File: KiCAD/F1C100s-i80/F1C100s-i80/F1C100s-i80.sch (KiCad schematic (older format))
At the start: 98 parts, among them J1 LCD_I8080_CONNECTOR_16x2-DIP, J10 USB_B_Micro, J2 Key Export, J3 SPK, J4 LRADC, J5 UART, J6 Touch, J7 Power, J8 Micro_SD_Card, J9 USB_A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

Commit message: c100s
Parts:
- J2: footprint Connector_PinHeader_2.54mm:PinHeader_1x08_P2.54mm_Horizontal -> Connector_PinHeader_2.54mm:PinHeader_1x07_P2.54mm_Horizontal
- R25, R26, R28, R29: value 0R -> 22R
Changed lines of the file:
@@
 P 10250 4750
 F 0 "R25" V 10200 4650 50  0000 C CNN
-F 1 "0R" V 10250 4750 50  0000 C CNN
+F 1 "22R" V 10250 4750 50  0000 C CNN
 F 2 "Resistor_SMD:R_0603_1608Metric_Pad1.05x0.95mm_HandSolder" H 10250 4750 50  0001 C CNN
 F 3 "~" H 10250 4750 50  0001 C CNN
@@
 P 10450 5550
 F 0 "R28" V 10400 5450 50  0000 C CNN
-F 1 "0R" V 10450 5550 50  0000 C CNN
+F 1 "22R" V 10450 5550 50  0000 C CNN
 F 2 "Resistor_SMD:R_0603_1608Metric_Pad1.05x0.95mm_HandSolder" H 10450 5550 50  0001 C CNN
 F 3 "~" H 10450 5550 50  0001 C CNN
@@
 P 10450 5650
 F 0 "R29" V 10400 5550 50  0000 C CNN
-F 1 "0R" V 10450 5650 50  0000 C CNN
+F 1 "22R" V 10450 5650 50  0000 C CNN
 F 2 "Resistor_SMD:R_0603_1608Metric_Pad1.05x0.95mm_HandSolder" H 10450 5650 50  0001 C CNN
 F 3 "~" H 10450 5650 50  0001 C CNN
@@
 P 10250 4850
 F 0 "R26" V 10200 4750 50  0000 C CNN
-F 1 "0R" V 10250 4850 50  0000 C CNN
+F 1 "22R" V 10250 4850 50  0000 C CNN
 F 2 "Resistor_SMD:R_0603_1608Metric_Pad1.05x0.95mm_HandSolder" H 10250 4850 50  0001 C CNN
 F 3 "~" H 10250 4850 50  0001 C CNN
@@
 F 0 "J2" H 6950 3300 50  0000 C CNN
 F 1 "Key Export" H 7200 2450 50  0000 C CNN
-F 2 "Connector_PinHeader_2.54mm:PinHeader_1x08_P2.54mm_Horizontal" H 7000 2950 50  0001 C CNN
+F 2 "Connector_PinHeader_2.54mm:PinHeader_1x07_P2.54mm_Horizontal" H 7000 2950 50  0001 C CNN
 F 3 "~" H 7000 2950 50  0001 C CNN
 	1    7000 2950

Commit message: c100s&f40x
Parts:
- BT1: footprint Battery:BatteryHolder_Keystone_3000_1x12mm -> qmechanics:CR1220-2
- J2: footprint Connector_PinHeader_2.54mm:PinHeader_1x07_P2.54mm_Horizontal -> Connector_PinHeader_2.54mm:PinHeader_1x08_P2.54mm_Horizontal
- J9: footprint qconnectors:USB-AF -> qconnectors:USB-AF90
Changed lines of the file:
@@
 F 0 "J9" H 11200 5100 50  0000 R CNN
 F 1 "USB_A" H 11250 4400 50  0000 R CNN
-F 2 "qconnectors:USB-AF" H 11100 4700 50  0001 C CNN
+F 2 "qconnectors:USB-AF90" H 11100 4700 50  0001 C CNN
 F 3 " ~" H 11100 4700 50  0001 C CNN
 	1    10950 4750
@@
 F 0 "BT1" H 6458 4946 50  0000 L CNN
 F 1 "Battery" H 6458 4855 50  0000 L CNN
-F 2 "Battery:BatteryHolder_Keystone_3000_1x12mm" V 6350 4960 50  0001 C CNN
+F 2 "qmechanics:CR1220-2" V 6350 4960 50  0001 C CNN
 F 3 "~" V 6350 4960 50  0001 C CNN
 	1    6350 4900
@@
 F 0 "J2" H 6950 3300 50  0000 C CNN
 F 1 "Key Export" H 7200 2450 50  0000 C CNN
-F 2 "Connector_PinHeader_2.54mm:PinHeader_1x07_P2.54mm_Horizontal" H 7000 2950 50  0001 C CNN
+F 2 "Connector_PinHeader_2.54mm:PinHeader_1x08_P2.54mm_Horizontal" H 7000 2950 50  0001 C CNN
 F 3 "~" H 7000 2950 50  0001 C CNN
 	1    7000 2950

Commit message: 修改DCDC部分
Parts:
- C21, C22, C23: footprint Capacitor_SMD:C_0603_1608Metric_Pad1.05x0.95mm_HandSolder -> Capacitor_SMD:C_1206_3216Metric_Pad1.42x1.75mm_HandSolder
- J10: footprint Connector_USB:USB_Micro-B_Wuerth_629105150521 -> qconnectors:USB_Micro
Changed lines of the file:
@@
 EESchema Schematic File Version 4
-LIBS:F1C100s-i80-cache
 EELAYER 30 0
 EELAYER END
@@
 F 0 "C21" H 9100 900 50  0000 L CNN
 F 1 "10uF" H 9100 800 50  0000 L CNN
-F 2 "Capacitor_SMD:C_0603_1608Metric_Pad1.05x0.95mm_HandSolder" H 9100 850 50  0001 C CNN
+F 2 "Capacitor_SMD:C_1206_3216Metric_Pad1.42x1.75mm_HandSolder" H 9100 850 50  0001 C CNN
 F 3 "~" H 9100 850 50  0001 C CNN
 	1    9100 850
@@
 F 0 "C22" H 9100 1400 50  0000 L CNN
 F 1 "10uF" H 9100 1300 50  0000 L CNN
-F 2 "Capacitor_SMD:C_0603_1608Metric_Pad1.05x0.95mm_HandSolder" H 9100 1350 50  0001 C CNN
+F 2 "Capacitor_SMD:C_1206_3216Metric_Pad1.42x1.75mm_HandSolder" H 9100 1350 50  0001 C CNN
 F 3 "~" H 9100 1350 50  0001 C CNN
 	1    9100 1350
@@
 F 0 "C23" H 9100 1900 50  0000 L CNN
 F 1 "10uF" H 9100 1800 50  0000 L CNN
-F 2 "Capacitor_SMD:C_0603_1608Metric_Pad1.05x0.95mm_HandSolder" H 9100 1850 50  0001 C CNN
+F 2 "Capacitor_SMD:C_1206_3216Metric_Pad1.42x1.75mm_HandSolder" H 9100 1850 50  0001 C CNN
 F 3 "~" H 9100 1850 50  0001 C CNN
 	1    9100 1850
@@
 F 0 "J10" H 11200 5900 50  0000 R CNN
 F 1 "USB_B_Micro" H 11500 5200 50  0000 R CNN
-F 2 "Connector_USB:USB_Micro-B_Wuerth_629105150521" H 11100 5500 50  0001 C CNN
+F 2 "qconnectors:USB_Micro" H 11100 5500 50  0001 C CNN
 F 3 "~" H 11100 5500 50  0001 C CNN
 	1    10950 5550

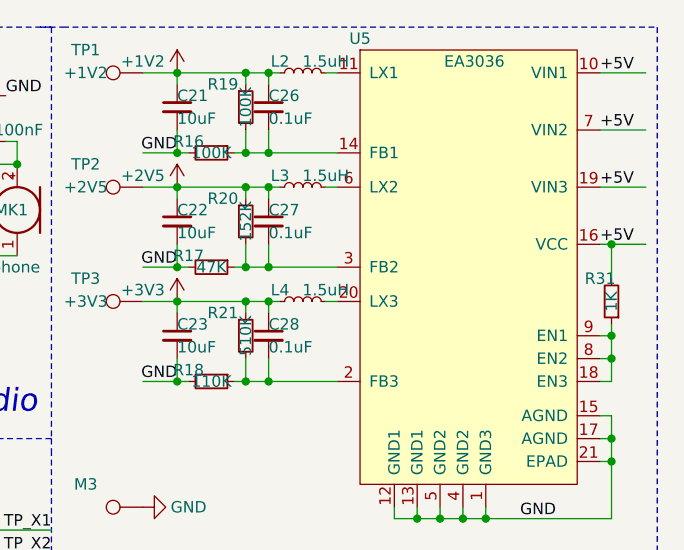
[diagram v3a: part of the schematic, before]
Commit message: 更改C100s走线
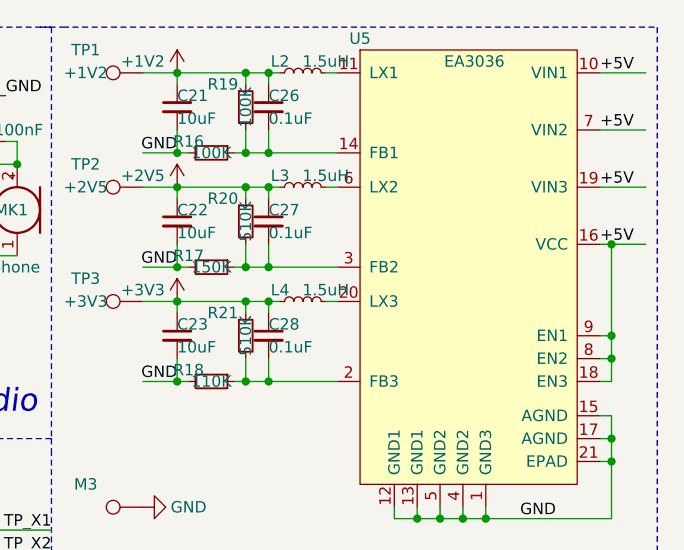
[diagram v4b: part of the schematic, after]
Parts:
- removed R31: 1K, Resistor_SMD:R_0603_1608Metric_Pad1.05x0.95mm_HandSolder, symbol Device:R_Small
- R17: value 47K -> 150K
- R20: value 152K -> 510K
- RN1: footprint Resistor_SMD:R_Cat16-4 -> Resistor_SMD:R_Array_Convex_4x0603
- U5: footprint qchip:EA3036-QFN-20_EP_3.55x3.55_Pitch0.4mm -> qchip:EA3036-QFN-20_EP_3.55x3.55_Pitch0.4mm_Handsoldering
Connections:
- wire segments 325 -> 324
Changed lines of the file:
@@
 F 0 "U5" H 9900 3150 50  0000 C CNN
 F 1 "EA3036" H 10400 3050 50  0000 C CNN
-F 2 "qchip:EA3036-QFN-20_EP_3.55x3.55_Pitch0.4mm" H 8250 1850 50  0001 C CNN
+F 2 "qchip:EA3036-QFN-20_EP_3.55x3.55_Pitch0.4mm_Handsoldering" H 8250 1850 50  0001 C CNN
 F 3 "" H 8250 1850 50  0001 C CNN
 	1    10350 1850
 	1    0    0    -1
 $EndComp
-$Comp
-L Device:R_Small R31
-U 1 1 5DF74049
-P 11000 1700
-F 0 "R31" H 11050 1600 50  0000 C CNN
-F 1 "1K" V 11000 1700 50  0000 C CNN
-F 2 "Resistor_SMD:R_0603_1608Metric_Pad1.05x0.95mm_HandSolder" H 11000 1700 50  0001 C CNN
-F 3 "~" H 11000 1700 50  0001 C CNN
-	1    11000 1700
-	-1   0    0    1
-$EndComp
 Wire Wire Line
 	10950 1850 11000 1850
@@
 Wire Wire Line
 	11000 1950 11000 1850
-Wire Wire Line
-	11000 1850 11000 1800
 Text Label 10950 1200 0    50   ~ 0
 +5V
@@
 Text Label 10950 1450 0    50   ~ 0
 +5V
-Wire Wire Line
-	11000 1600 11000 1450
 Wire Wire Line
 	10950 1450 11000 1450
@@
 P 9400 1350
 F 0 "R20" H 9300 1450 50  0000 C CNN
-F 1 "152K" V 9400 1350 50  0000 C CNN
+F 1 "510K" V 9400 1350 50  0000 C CNN
 F 2 "Resistor_SMD:R_0603_1608Metric_Pad1.05x0.95mm_HandSolder" H 9400 1350 50  0001 C CNN
 F 3 "~" H 9400 1350 50  0001 C CNN
@@
 P 9250 1550
 F 0 "R17" V 9200 1450 50  0000 C CNN
-F 1 "47K" V 9250 1550 50  0000 C CNN
+F 1 "150K" V 9250 1550 50  0000 C CNN
 F 2 "Resistor_SMD:R_0603_1608Metric_Pad1.05x0.95mm_HandSolder" H 9250 1550 50  0001 C CNN
 F 3 "~" H 9250 1550 50  0001 C CNN
@@
 F 0 "RN1" V 8450 4500 50  0000 C CNN
 F 1 "47K" V 8450 4650 50  0000 C CNN
-F 2 "Resistor_SMD:R_Cat16-4" V 9025 4650 50  0001 C CNN
+F 2 "Resistor_SMD:R_Array_Convex_4x0603" V 9025 4650 50  0001 C CNN
 F 3 "~" H 8750 4650 50  0001 C CNN
 	1    8750 4650
@@
 Text Label 7250 2950 0    50   ~ 0
 KEYX
+Wire Wire Line
+	11000 1450 11000 1850
 $EndSCHEMATC

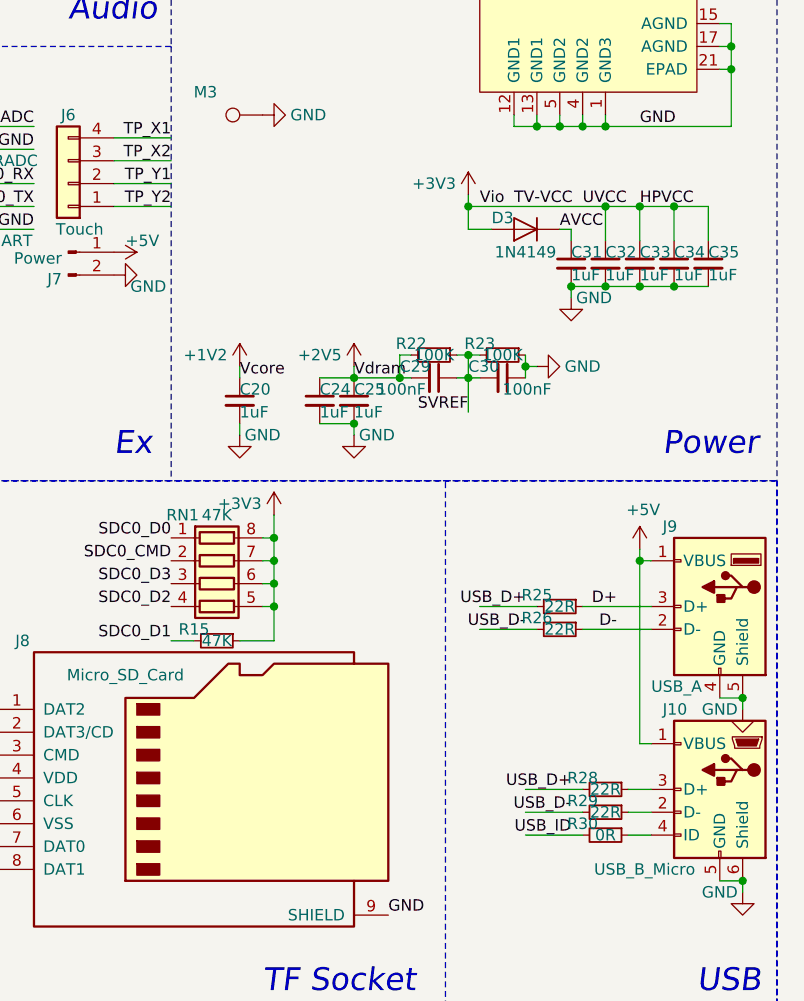
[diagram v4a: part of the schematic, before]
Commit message: 修改排阻为0603电阻
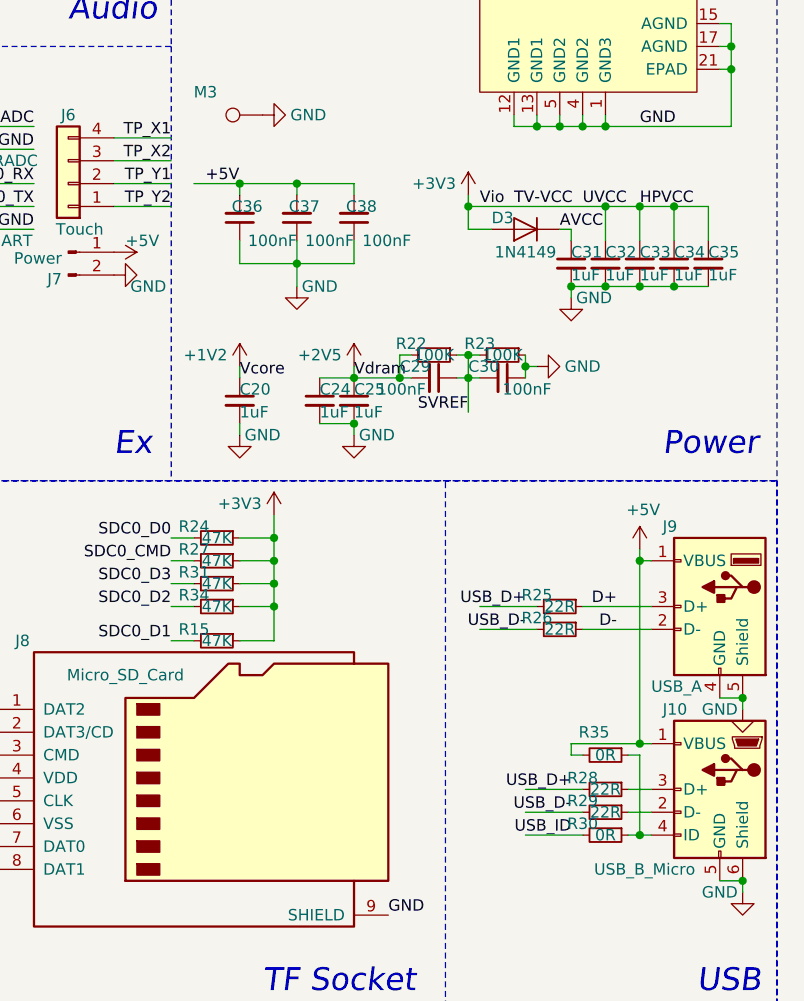
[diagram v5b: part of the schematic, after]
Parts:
- removed RN1: 47K, Resistor_SMD:R_Array_Convex_4x0603, symbol Device:R_Pack04
- added C36, C37, C38: 100nF, Capacitor_SMD:C_0603_1608Metric_Pad1.05x0.95mm_HandSolder, symbol Device:C_Small
- added R24, R27, R31, R34: 47K, Resistor_SMD:R_0603_1608Metric_Pad1.05x0.95mm_HandSolder, symbol Device:R_Small
- added R35: 0R, Resistor_SMD:R_0603_1608Metric_Pad1.05x0.95mm_HandSolder, symbol Device:R_Small
- U5: footprint qchip:EA3036-QFN-20_EP_3.55x3.55_Pitch0.4mm_Handsoldering -> qchip:EA3036-QFN-20_EP_3.55x3.55_Pitch0.4mm
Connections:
- wire segments 324 -> 346
